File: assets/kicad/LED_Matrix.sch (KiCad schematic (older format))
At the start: 82 parts

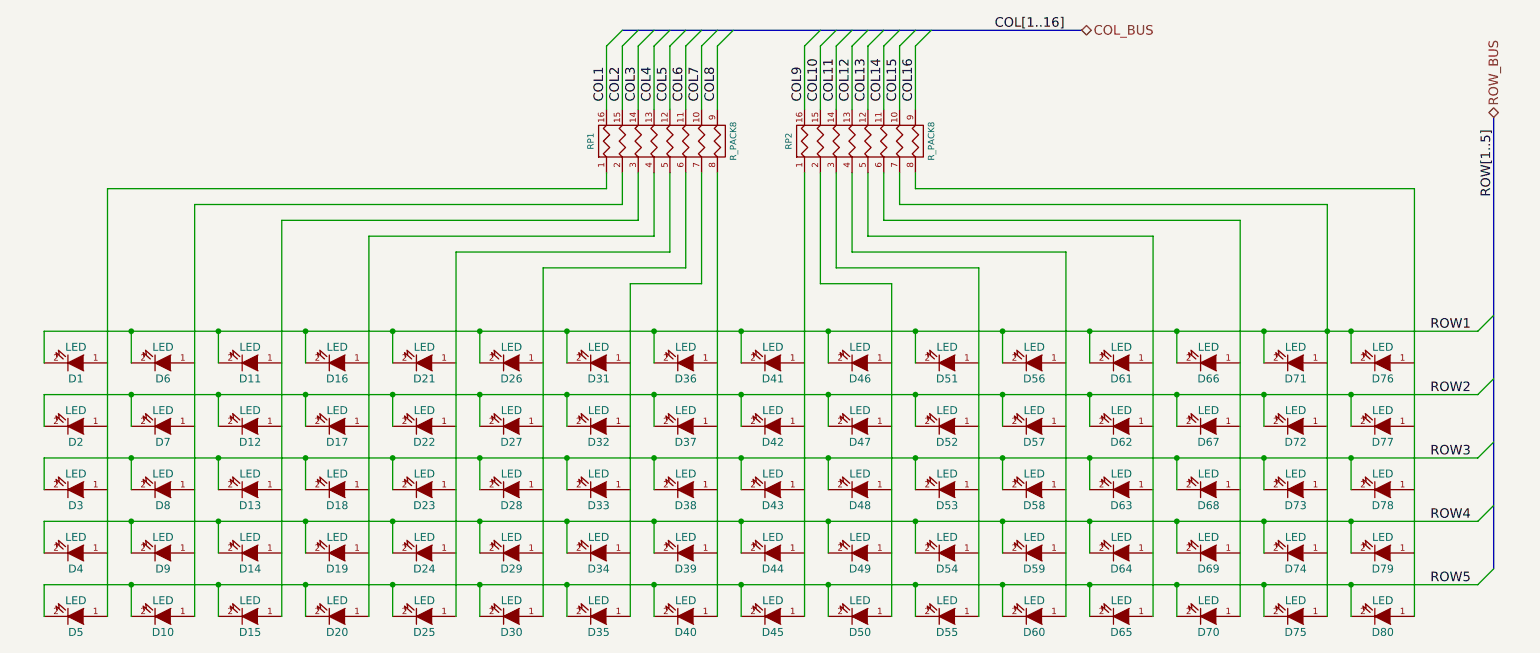
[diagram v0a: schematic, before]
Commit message: Cleaned up schematic. Edited README for clarity.
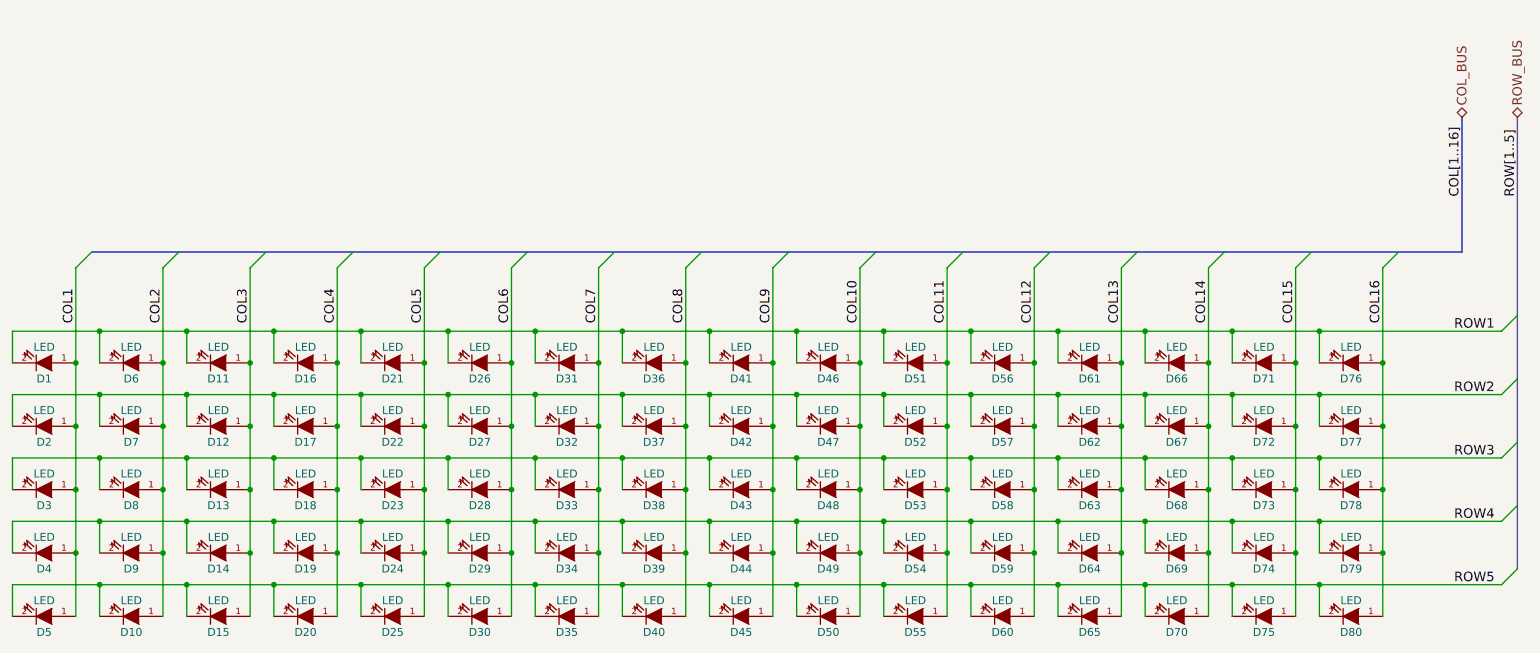
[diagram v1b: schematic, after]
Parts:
- removed RP1, RP2: R_PACK8, ~, symbol R_PACK8
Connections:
- net COL1: now also D1.1 (A), D2.1 (A), D3.1 (A), D4.1 (A), D5.1 (A)
- net COL10: now also D46.1 (A), D47.1 (A), D48.1 (A), D49.1 (A), D50.1 (A)
- net COL11: now also D51.1 (A), D52.1 (A), D53.1 (A), D54.1 (A), D55.1 (A)
- net COL12: now also D56.1 (A), D57.1 (A), D58.1 (A), D59.1 (A), D60.1 (A)
- net COL13: now also D61.1 (A), D62.1 (A), D63.1 (A), D64.1 (A), D65.1 (A)
- net COL14: now also D66.1 (A), D67.1 (A), D68.1 (A), D69.1 (A), D70.1 (A)
- net COL15: now also D71.1 (A), D72.1 (A), D73.1 (A), D74.1 (A), D75.1 (A)
- net COL16: now also D76.1 (A), D77.1 (A), D78.1 (A), D79.1 (A), D80.1 (A)
- net COL2: now also D10.1 (A), D6.1 (A), D7.1 (A), D8.1 (A), D9.1 (A)
- net COL3: now also D11.1 (A), D12.1 (A), D13.1 (A), D14.1 (A), D15.1 (A)
- net COL4: now also D16.1 (A), D17.1 (A), D18.1 (A), D19.1 (A), D20.1 (A)
- net COL5: now also D21.1 (A), D22.1 (A), D23.1 (A), D24.1 (A), D25.1 (A)
- net COL6: now also D26.1 (A), D27.1 (A), D28.1 (A), D29.1 (A), D30.1 (A)
- net COL7: now also D31.1 (A), D32.1 (A), D33.1 (A), D34.1 (A), D35.1 (A)
- net COL8: now also D36.1 (A), D37.1 (A), D38.1 (A), D39.1 (A), D40.1 (A)
- net COL9: now also D41.1 (A), D42.1 (A), D43.1 (A), D44.1 (A), D45.1 (A)
- net ROW1: no longer D75.1 (A)
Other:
- moved on the sheet: D1, D10, D11, D12, D13, D14, D15, D16, D17, D18, D19, D2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
